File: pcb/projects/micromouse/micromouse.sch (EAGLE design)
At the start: 44 parts, among them IC1 UA78M33DCY, IC2 UA78M05DCY, M1 332-06, M2 332-06, U1 DSPIC33FJ64MC804-H/PT

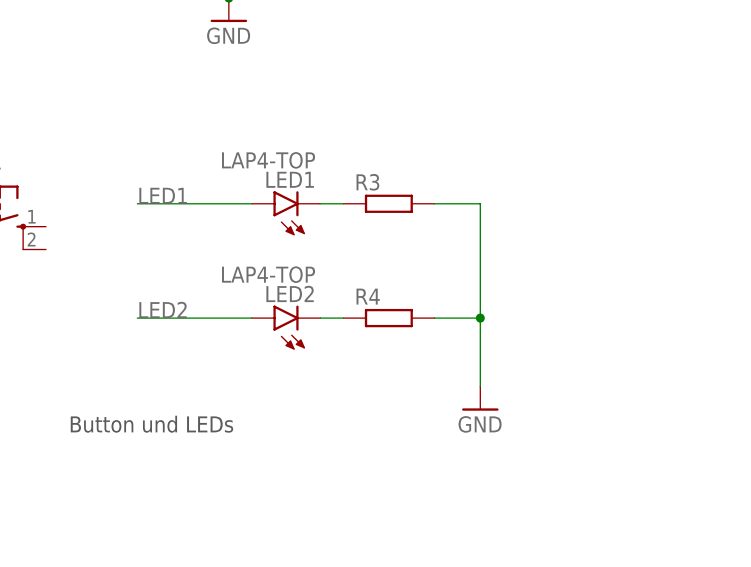
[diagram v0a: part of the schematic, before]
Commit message: Add value for resistors for LEDs
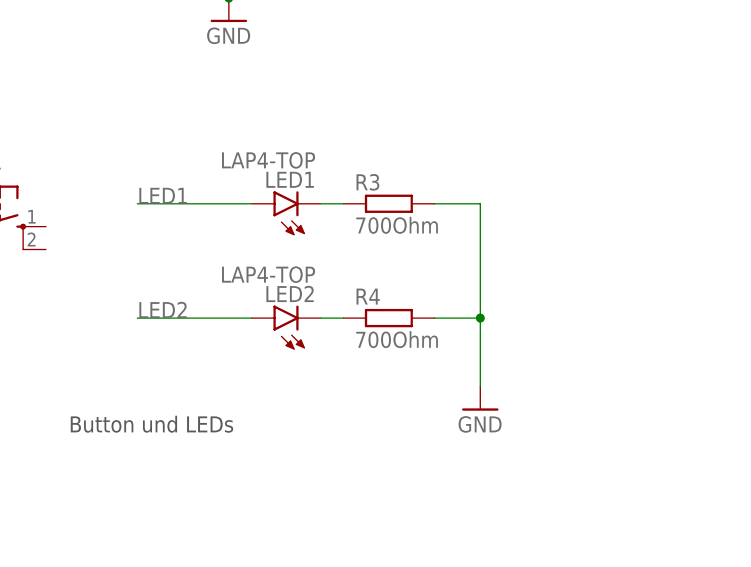
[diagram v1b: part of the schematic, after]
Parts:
- R3, R4: value (none) -> 700Ohm
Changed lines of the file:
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@@
 <part name="LED1" library="led" library_urn="urn:adsk.eagle:library:259" deviceset="*P4" device="-TOP" package3d_urn="urn:adsk.eagle:package:15879/1" technology="LA"/>
 <part name="LED2" library="led" library_urn="urn:adsk.eagle:library:259" deviceset="*P4" device="-TOP" package3d_urn="urn:adsk.eagle:package:15879/1" technology="LA"/>
-<part name="R3" library="rcl" library_urn="urn:adsk.eagle:library:334" deviceset="R-EU_" device="R0805" package3d_urn="urn:adsk.eagle:package:23553/2"/>
-<part name="R4" library="rcl" library_urn="urn:adsk.eagle:library:334" deviceset="R-EU_" device="R0805" package3d_urn="urn:adsk.eagle:package:23553/2"/>
+<part name="R3" library="rcl" library_urn="urn:adsk.eagle:library:334" deviceset="R-EU_" device="R0805" package3d_urn="urn:adsk.eagle:package:23553/2" value="700Ohm"/>
+<part name="R4" library="rcl" library_urn="urn:adsk.eagle:library:334" deviceset="R-EU_" device="R0805" package3d_urn="urn:adsk.eagle:package:23553/2" value="700Ohm"/>
 <part name="GND20" library="supply1" library_urn="urn:adsk.eagle:library:371" deviceset="GND" device=""/>
 <part name="C7" library="rcl" library_urn="urn:adsk.eagle:library:334" deviceset="C-EU" device="C0805" package3d_urn="urn:adsk.eagle:package:23617/2" value="100nF"/>

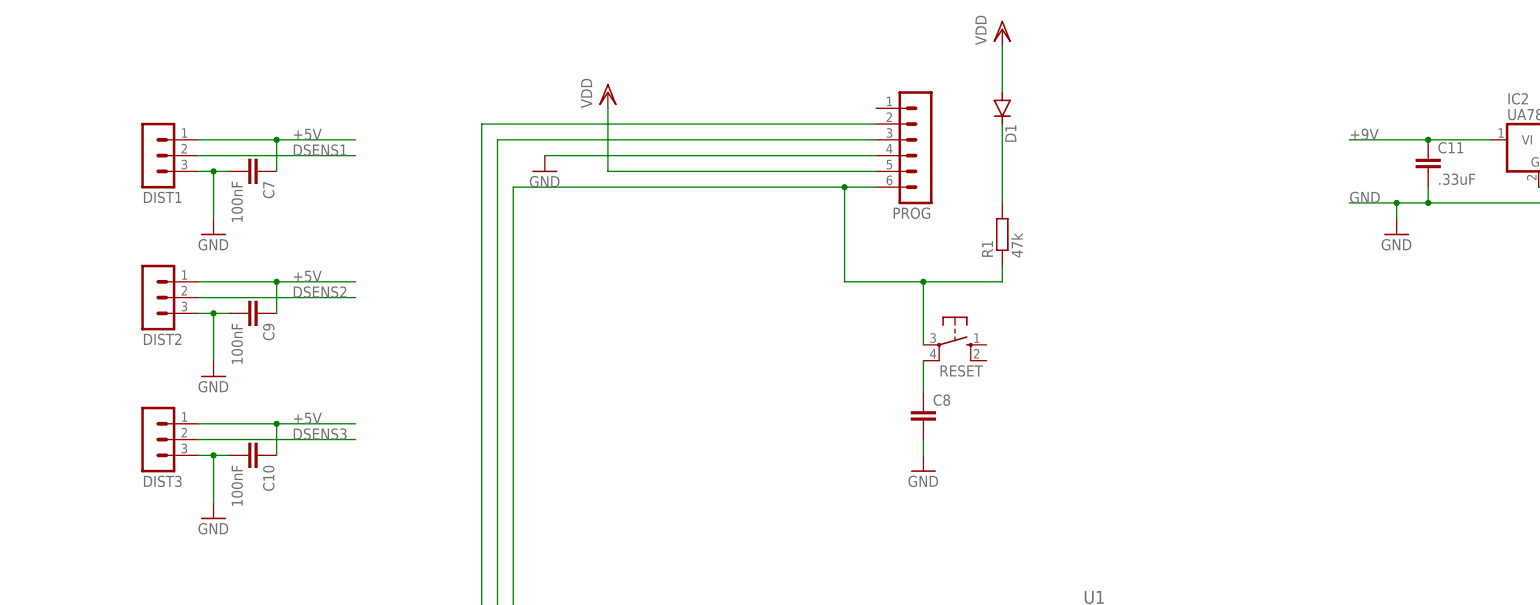
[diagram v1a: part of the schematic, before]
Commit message: Add solder pad for distance sensor and battery
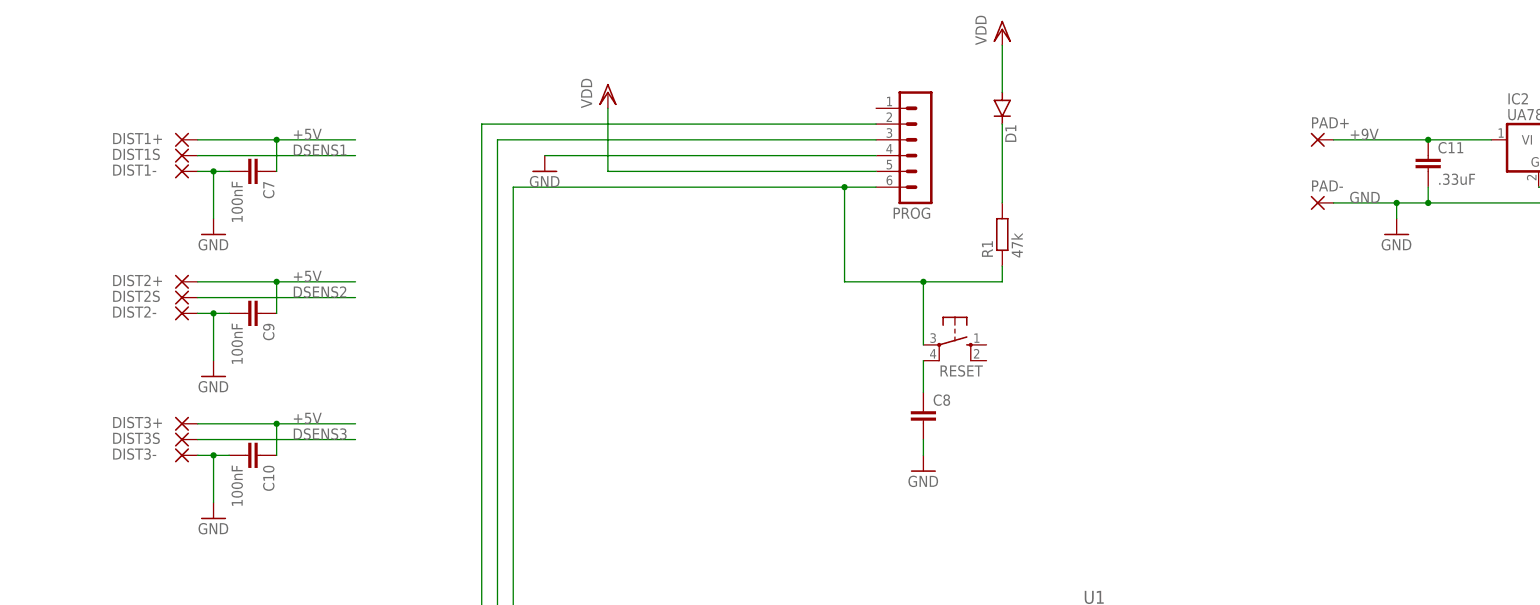
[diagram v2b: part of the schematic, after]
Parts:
- removed DIST1, DIST2, DIST3: (no value), con-lstb:MA03-1
- added DIST1+, DIST1-, DIST1S, DIST2+, DIST2-, DIST2S, DIST3+, DIST3-, DIST3S, PAD+, PAD-: (no value), wirepad:SMD2
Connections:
- net +5V: now also DIST1+.P, DIST2+.P, DIST3+.P; no longer DIST1.1, DIST2.1, DIST3.1
- net +9V: now also PAD+.P
- net DSENS1: now also DIST1S.P; no longer DIST1.2
- net DSENS2: now also DIST2S.P; no longer DIST2.2
- net DSENS3: now also DIST3S.P; no longer DIST3.2
- net GND: now also DIST1-.P, DIST2-.P, DIST3-.P, PAD-.P; no longer DIST1.3, DIST2.3, DIST3.3

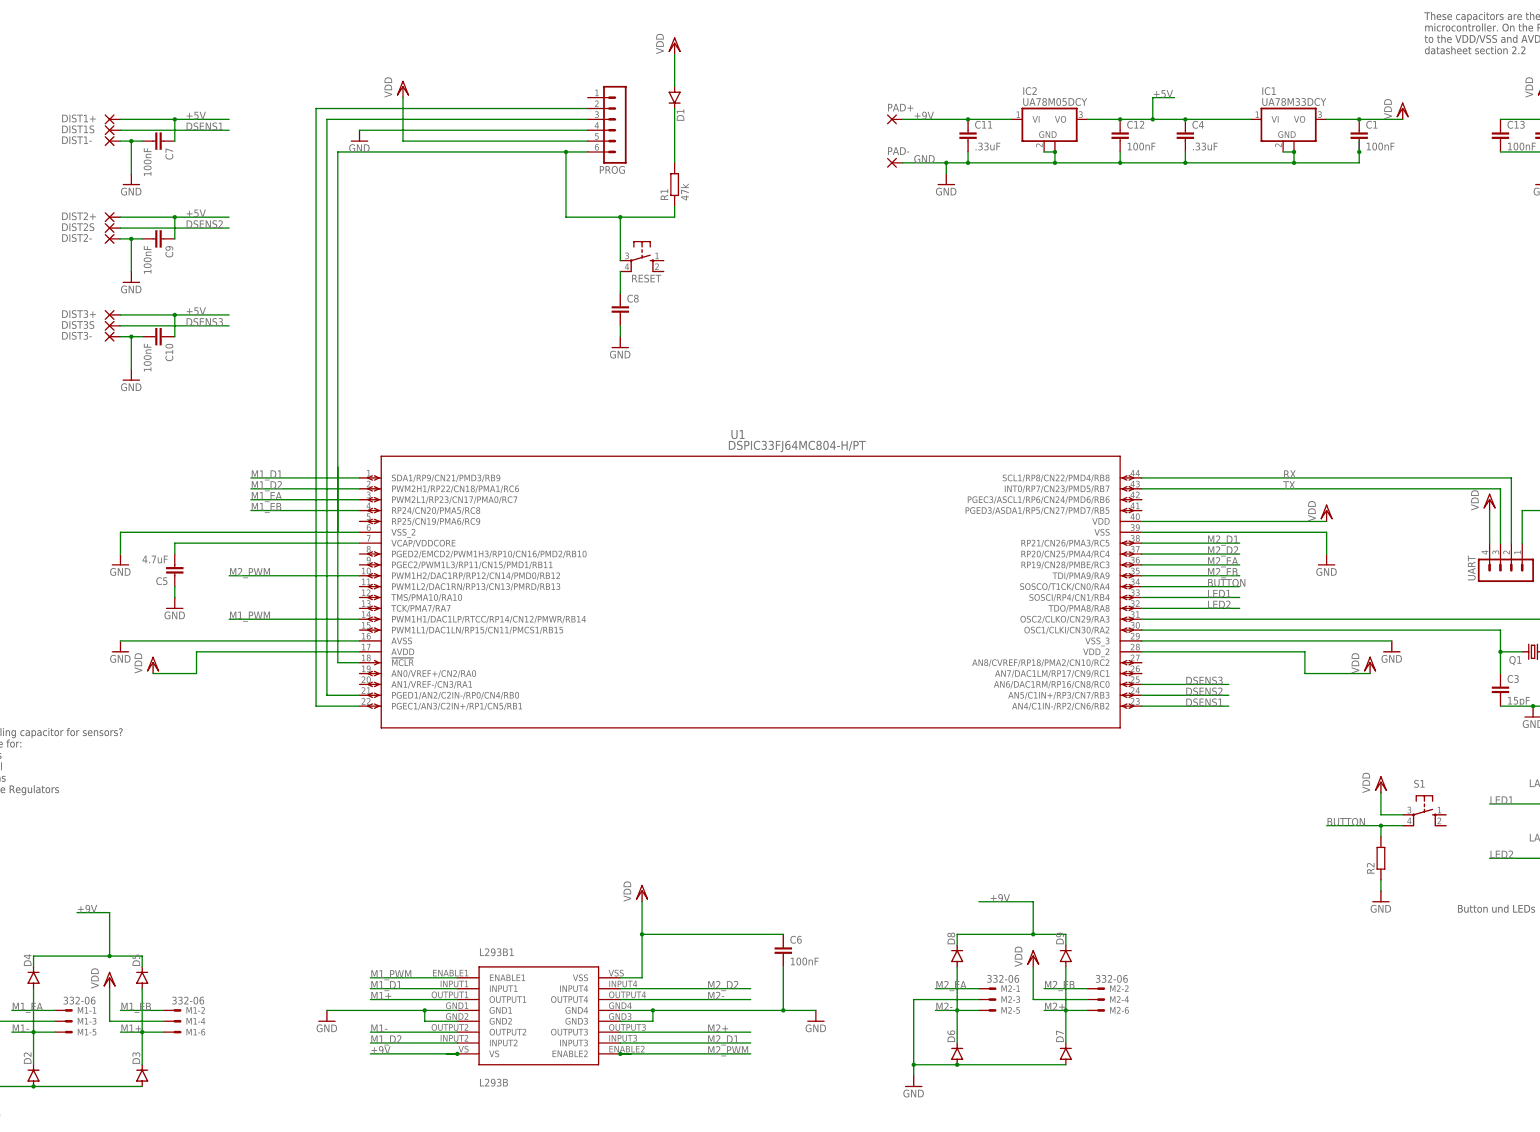
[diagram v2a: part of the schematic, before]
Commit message: Use TO-220 for voltage reguators
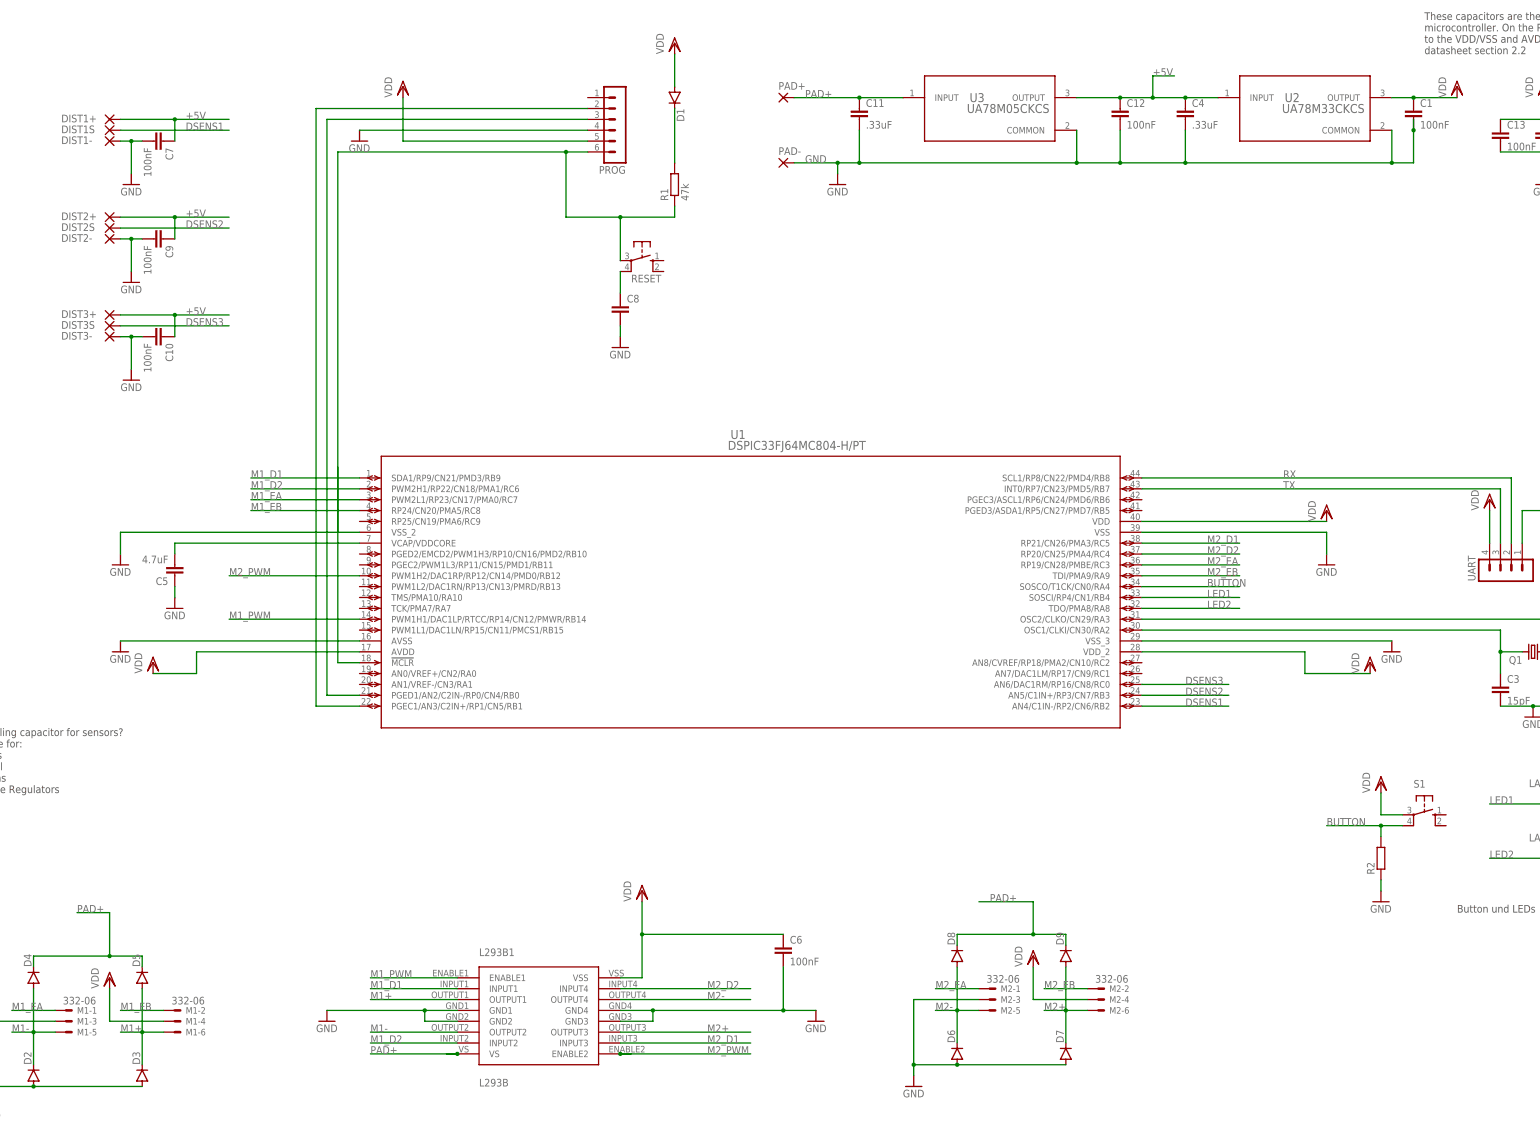
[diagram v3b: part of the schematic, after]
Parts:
- removed IC1: UA78M33DCY, linear:UA78M33DCY
- removed IC2: UA78M05DCY, linear:UA78M05DCY
- added U2: UA78M33CKCS, micromouse:UA78M33CKCS
- added U3: UA78M05CKCS, micromouse:UA78M05CKCS
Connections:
- removed net +9V: C11.1, D4.C, D5.C, D8.C, D9.C, IC2.VI, L293B1.VS, PAD+.P
- new net PAD+: C11.1, D4.C, D5.C, D8.C, D9.C, L293B1.VS, PAD+.P, U3.INPUT
- net +5V: now also U2.INPUT, U3.OUTPUT; no longer IC1.VI, IC2.VO
- net GND: now also U2.COMMON, U3.COMMON; no longer IC1.GND, IC1.GND@1, IC2.GND, IC2.GND@1
- net VDD: now also U2.OUTPUT; no longer IC1.VO
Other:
- moved on the sheet: C1, C11, C12, C4, PAD+, PAD-

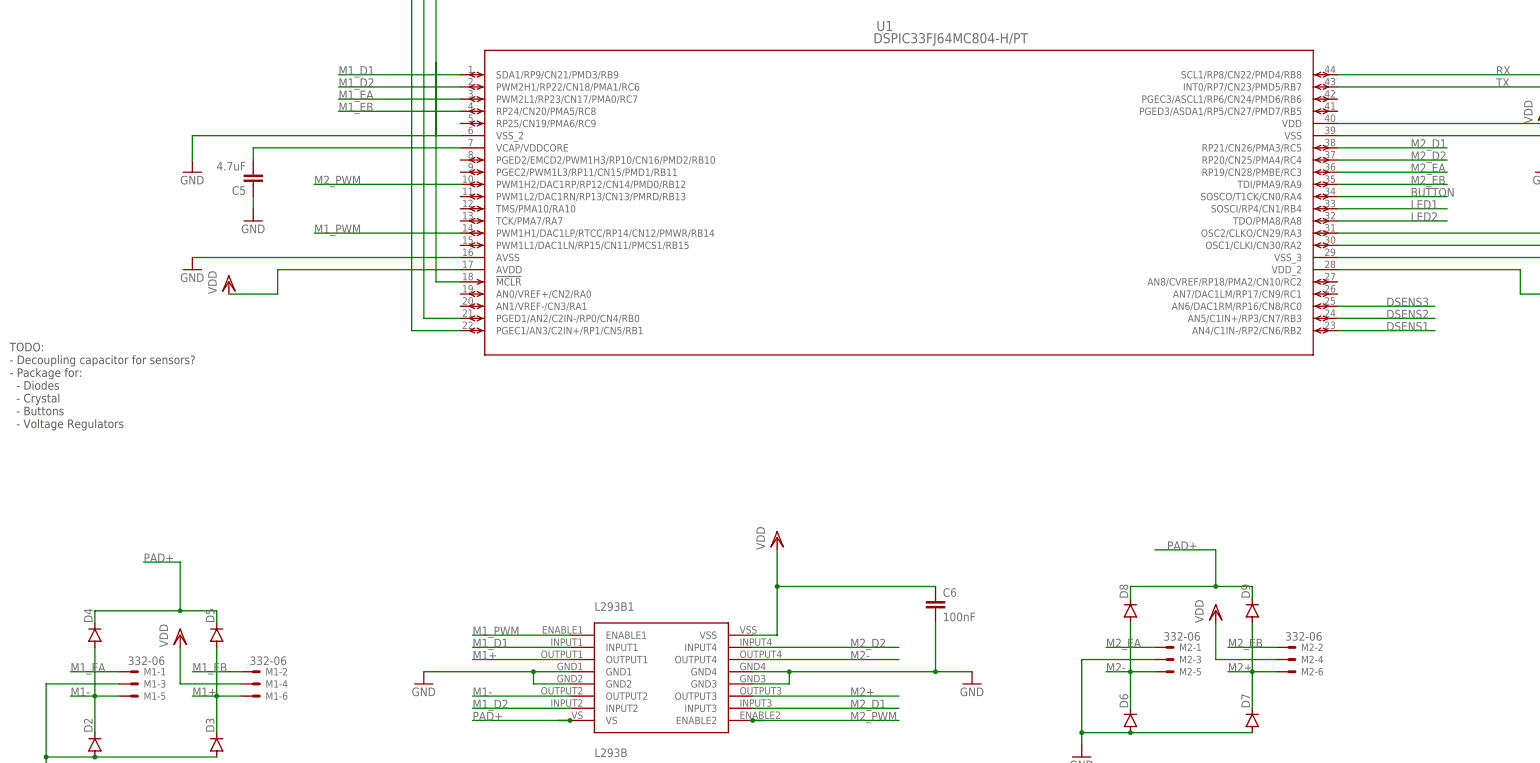
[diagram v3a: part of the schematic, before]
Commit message: Position components
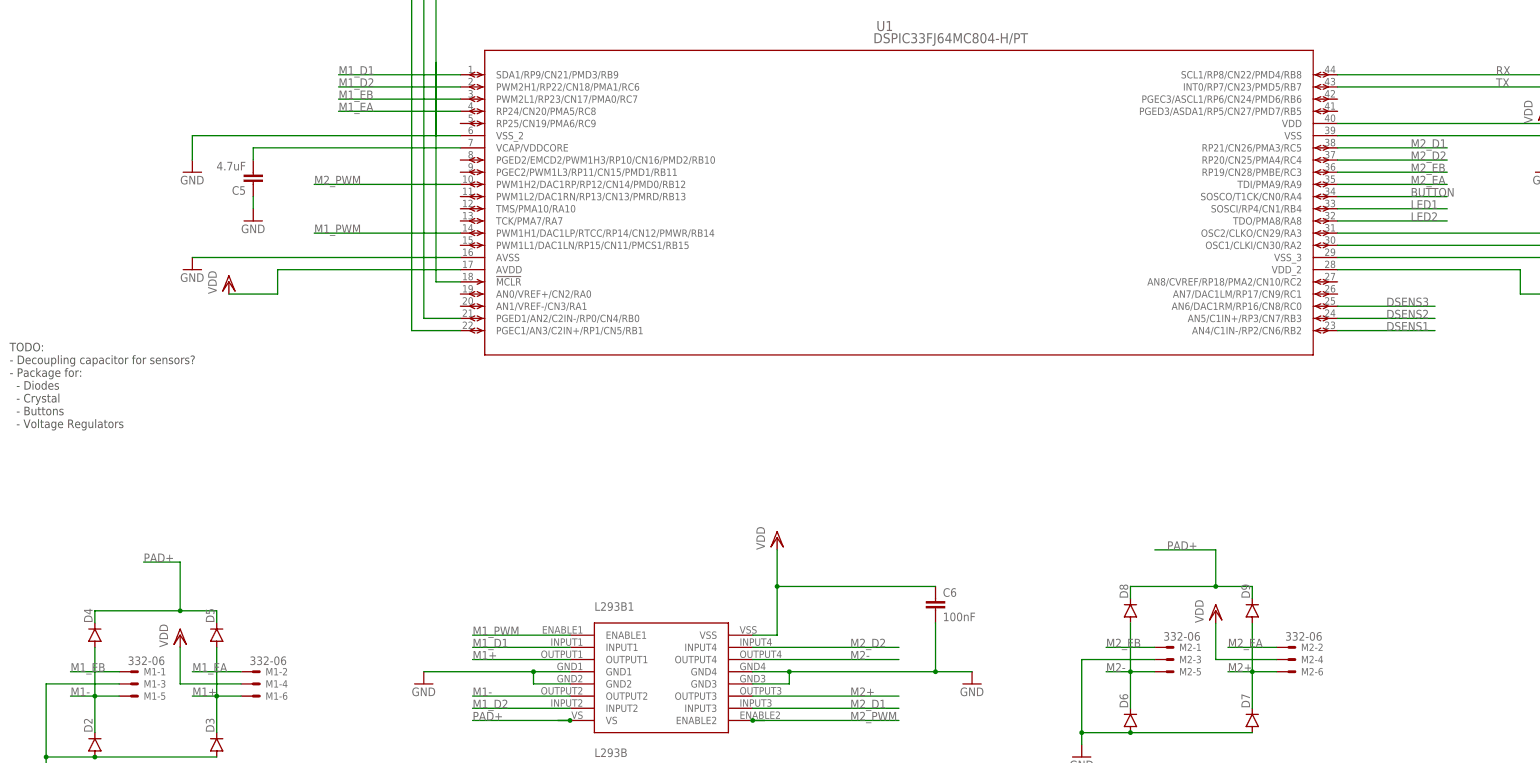
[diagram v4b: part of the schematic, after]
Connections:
- net M1_EA: now also M1-2.S, U1.RP24/CN20/PMA5/RC8; no longer M1-1.S, U1.PWM2L1/RP23/CN17/PMA0/RC7
- net M1_EB: now also M1-1.S, U1.PWM2L1/RP23/CN17/PMA0/RC7; no longer M1-2.S, U1.RP24/CN20/PMA5/RC8
- net M2_EA: now also M2-2.S, U1.TDI/PMA9/RA9; no longer M2-1.S, U1.RP19/CN28/PMBE/RC3
- net M2_EB: now also M2-1.S, U1.RP19/CN28/PMBE/RC3; no longer M2-2.S, U1.TDI/PMA9/RA9
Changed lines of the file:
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@@
 </segment>
 </net>
-<net name="M1_EA" class="0">
+<net name="M1_EB" class="0">
 <segment>
 <pinref part="M1" gate="-1" pin="S"/>
@@
 </segment>
 </net>
-<net name="M1_EB" class="0">
+<net name="M1_EA" class="0">
 <segment>
 <pinref part="M1" gate="-2" pin="S"/>
@@
 </segment>
 </net>
-<net name="M2_EA" class="0">
+<net name="M2_EB" class="0">
 <segment>
 <pinref part="M2" gate="-1" pin="S"/>
@@
 </segment>
 </net>
-<net name="M2_EB" class="0">
+<net name="M2_EA" class="0">
 <segment>
 <pinref part="M2" gate="-2" pin="S"/>
